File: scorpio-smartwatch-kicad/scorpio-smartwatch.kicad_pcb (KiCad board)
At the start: 2 copper layers, 5 parts, among them IC1 LSM6DSV80XTR, U1 nRF52840, U2 MIA-M10Q, U3 LIS2MDL

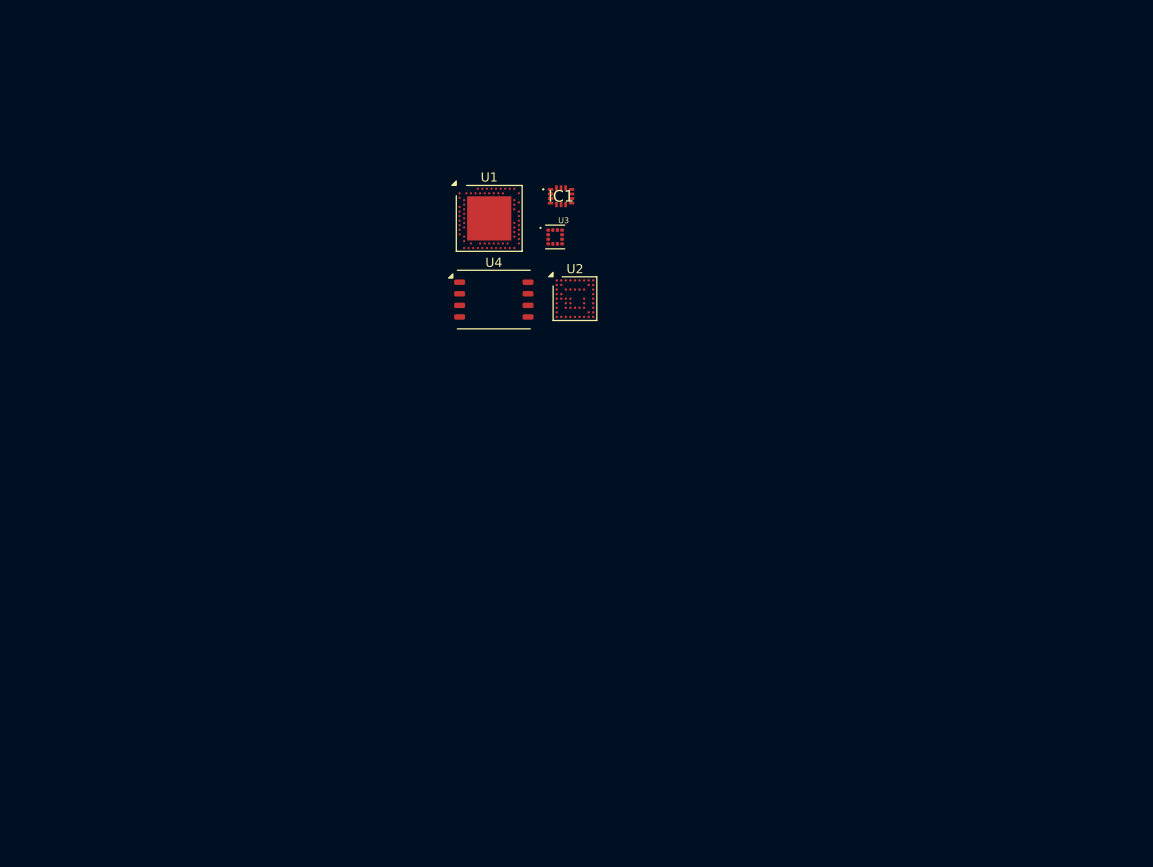
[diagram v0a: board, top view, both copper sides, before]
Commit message: Adding dimensions on the pcb and adding tables for current and battery sizes. need to change NRF footprint still. Need to add: Buttons, Screen Connector / Driver, HR connector (I2C), Power Management, Battery Connector, Mounting Holes, Passives.
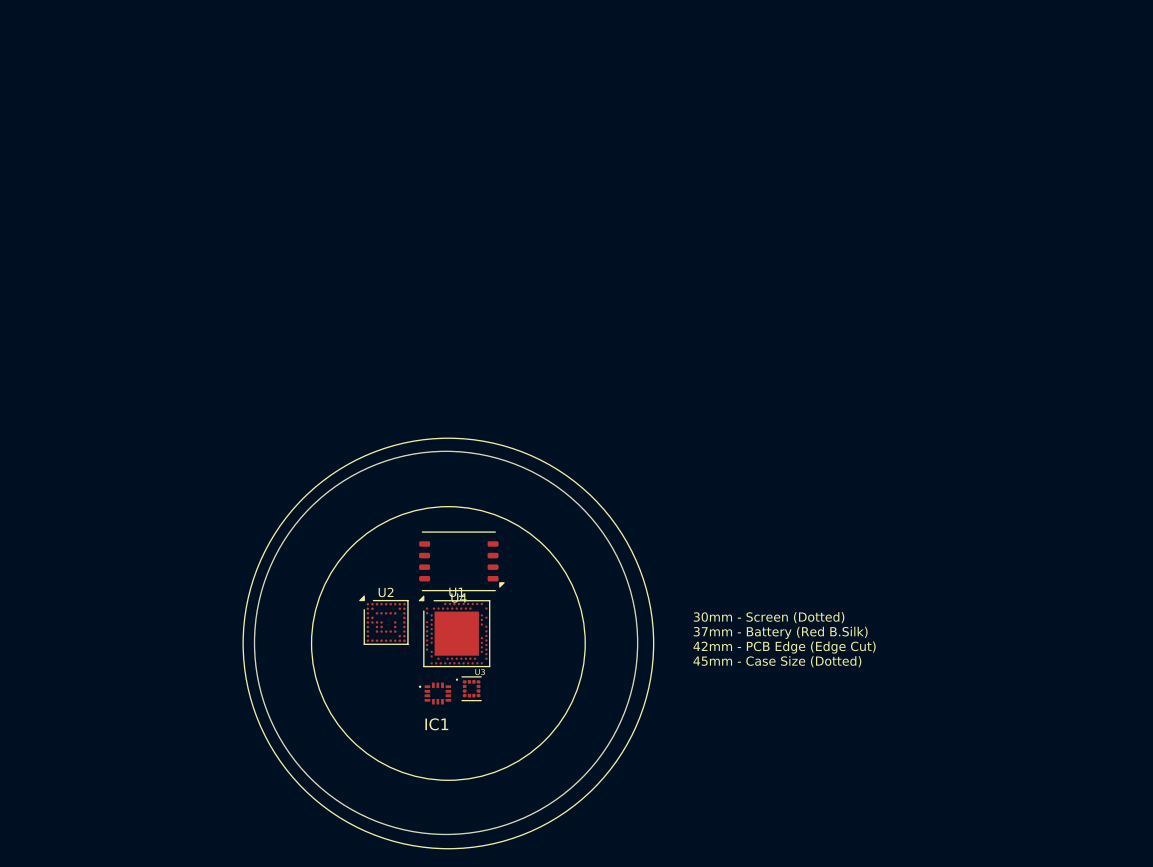
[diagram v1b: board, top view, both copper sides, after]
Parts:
- moved IC1 56.2 mm to (126.1, 132.7)
- moved U3 50.4 mm to (129.8, 132.2)
- moved U1 45.7 mm to (128.2, 126.2)
- moved U2 41.1 mm to (120.4, 124.9)
- moved U4 29.0 mm to (128.4, 118.2), turned to 180 degrees
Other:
- board outline added: 42 x 42 mm
- board text added: "30mm - Screen (Dotted) 37mm - Battery (Red B.Silk) 42mm - PCB Edge (Edge Cut) 45mm - Case Size (Dotted)"
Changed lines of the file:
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@@
 	(footprint "Package_LGA:ublox_LGA-53_4.5x4.5mm_Layout9x9_P0.5mm"
 		(layer "F.Cu")
-		(at 141.129 89.44)
+		(at 120.428 124.936)
 		(descr "ublox MIA SoC Module, 4.5x4.5mm, 53 Ball, 9x9 Layout, 0.5mm Pitch, generated with kicad-footprint-generator ipc_bga_generator.py, https://content.u-blox.com/sites/default/files/documents/MIA-M10Q_IntegrationManual_UBX-21028173.pdf#page=82")
 		(tags "LGA 53 0.5 ublox_MIA-M-LGA53")
@@
 	(footprint "Package_DFN_QFN:Nordic_AQFN-73-1EP_7x7mm_P0.5mm"
 		(layer "F.Cu")
-		(at 131.729 80.64)
+		(at 128.171 126.163)
 		(descr "http://infocenter.nordicsemi.com/index.jsp?topic=%2Fcom.nordic.infocenter.nrf52%2Fdita%2Fnrf52%2Fchips%2Fnrf52840.html")
 		(tags "AQFN 7mm ")
@@
 	(footprint "ZDSD16GLGIAG:LGA-8_8x6.2mm_P1.27mm"
 		(layer "F.Cu")
-		(at 132.234 89.54)
+		(at 128.397 118.237 180)
 		(descr "LGA, 8 Pin (https://datasheet.lcsc.com/lcsc/2303241700_Zetta-ZDSD64GLGEAG-R_C5277948.pdf#page=17), generated with kicad-footprint-generator ipc_noLead_generator.py")
 		(tags "LGA NoLead")
@@
 		(attr smd)
 		(fp_line
+			(start -4 3.21)
+			(end 4 3.21)
+			(stroke
+				(width 0.12)
+				(type solid)
+			)
+			(layer "F.SilkS")
+		)
+		(fp_line
 			(start -4 -3.21)
 			(end 4 -3.21)
-			(stroke
-				(width 0.12)
-				(type solid)
-			)
-			(layer "F.SilkS")
-		)
-		(fp_line
-			(start -4 3.21)
-			(end 4 3.21)
 			(stroke
 				(width 0.12)
@@
 		)
 		(fp_line
+			(start 4.6 2.46)
+			(end 4.25 2.46)
+			(stroke
+				(width 0.05)
+				(type solid)
+			)
+			(layer "F.CrtYd")
+		)
+		(fp_line
+			(start 4.6 -2.46)
+			(end 4.6 2.46)
+			(stroke
+				(width 0.05)
+				(type solid)
+			)
+			(layer "F.CrtYd")
+		)
+		(fp_line
+			(start 4.25 3.35)
+			(end -4.25 3.35)
+			(stroke
+				(width 0.05)
+				(type solid)
+			)
+			(layer "F.CrtYd")
+		)
+		(fp_line
+			(start 4.25 2.46)
+			(end 4.25 3.35)
+			(stroke
+				(width 0.05)
+				(type solid)
+			)
+			(layer "F.CrtYd")
+		)
+		(fp_line
+			(start 4.25 -2.46)
+			(end 4.6 -2.46)
+			(stroke
+				(width 0.05)
+				(type solid)
+			)
+			(layer "F.CrtYd")
+		)
+		(fp_line
+			(start 4.25 -3.35)
+			(end 4.25 -2.46)
+			(stroke
+				(width 0.05)
+				(type solid)
+			)
+			(layer "F.CrtYd")
+		)
+		(fp_line
+			(start -4.25 3.35)
+			(end -4.25 2.46)
+			(stroke
+				(width 0.05)
+				(type solid)
+			)
+			(layer "F.CrtYd")
+		)
+		(fp_line
+			(start -4.25 2.46)
+			(end -4.6 2.46)
+			(stroke
+				(width 0.05)
+				(type solid)
+			)
+			(layer "F.CrtYd")
+		)
+		(fp_line
+			(start -4.25 -2.46)
+			(end -4.25 -3.35)
+			(stroke
+				(width 0.05)
+				(type solid)
+			)
+			(layer "F.CrtYd")
+		)
+		(fp_line
+			(start -4.25 -3.35)
+			(end 4.25 -3.35)
+			(stroke
+				(width 0.05)
+				(type solid)
+			)
+			(layer "F.CrtYd")
+		)
+		(fp_line
+			(start -4.6 2.46)
+			(end -4.6 -2.46)
+			(stroke
+				(width 0.05)
+				(type solid)
+			)
+			(layer "F.CrtYd")
+		)
+		(fp_line
 			(start -4.6 -2.46)
 			(end -4.25 -2.46)
-			(stroke
-				(width 0.05)
-				(type solid)
-			)
-			(layer "F.CrtYd")
-		)
-		(fp_line
-			(start -4.6 2.46)
-			(end -4.6 -2.46)
-			(stroke
-				(width 0.05)
-				(type solid)
-			)
-			(layer "F.CrtYd")
-		)
-		(fp_line
-			(start -4.25 -3.35)
-			(end 4.25 -3.35)
-			(stroke
-				(width 0.05)
-				(type solid)
-			)
-			(layer "F.CrtYd")
-		)
-		(fp_line
-			(start -4.25 -2.46)
-			(end -4.25 -3.35)
-			(stroke
-				(width 0.05)
-				(type solid)
-			)
-			(layer "F.CrtYd")
-		)
-		(fp_line
-			(start -4.25 2.46)
-			(end -4.6 2.46)
-			(stroke
-				(width 0.05)
-				(type solid)
-			)
-			(layer "F.CrtYd")
-		)
-		(fp_line
-			(start -4.25 3.35)
-			(end -4.25 2.46)
-			(stroke
-				(width 0.05)
-				(type solid)
-			)
-			(layer "F.CrtYd")
-		)
-		(fp_line
-			(start 4.25 -3.35)
-			(end 4.25 -2.46)
-			(stroke
-				(width 0.05)
-				(type solid)
-			)
-			(layer "F.CrtYd")
-		)
-		(fp_line
-			(start 4.25 -2.46)
-			(end 4.6 -2.46)
-			(stroke
-				(width 0.05)
-				(type solid)
-			)
-			(layer "F.CrtYd")
-		)
-		(fp_line
-			(start 4.25 2.46)
-			(end 4.25 3.35)
-			(stroke
-				(width 0.05)
-				(type solid)
-			)
-			(layer "F.CrtYd")
-		)
-		(fp_line
-			(start 4.25 3.35)
-			(end -4.25 3.35)
-			(stroke
-				(width 0.05)
-				(type solid)
-			)
-			(layer "F.CrtYd")
-		)
-		(fp_line
-			(start 4.6 -2.46)
-			(end 4.6 2.46)
-			(stroke
-				(width 0.05)
-				(type solid)
-			)
-			(layer "F.CrtYd")
-		)
-		(fp_line
-			(start 4.6 2.46)
-			(end 4.25 2.46)
 			(stroke
 				(width 0.05)
@@
 		)
 		(pad "1" smd roundrect
-			(at -3.75 -1.905)
+			(at -3.75 -1.905 180)
 			(size 1.2 0.6)
 			(layers "F.Cu" "F.Mask" "F.Paste")
@@
 		)
 		(pad "2" smd roundrect
-			(at -3.75 -0.635)
+			(at -3.75 -0.635 180)
 			(size 1.2 0.6)
 			(layers "F.Cu" "F.Mask" "F.Paste")
@@
 		)
 		(pad "3" smd roundrect
-			(at -3.75 0.635)
+			(at -3.75 0.635 180)
 			(size 1.2 0.6)
 			(layers "F.Cu" "F.Mask" "F.Paste")
@@
 		)
 		(pad "4" smd roundrect
-			(at -3.75 1.905)
+			(at -3.75 1.905 180)
 			(size 1.2 0.6)
 			(layers "F.Cu" "F.Mask" "F.Paste")
@@
 		)
 		(pad "5" smd roundrect
-			(at 3.75 1.905)
+			(at 3.75 1.905 180)
 			(size 1.2 0.6)
 			(layers "F.Cu" "F.Mask" "F.Paste")
@@
 		)
 		(pad "6" smd roundrect
-			(at 3.75 0.635)
+			(at 3.75 0.635 180)
 			(size 1.2 0.6)
 			(layers "F.Cu" "F.Mask" "F.Paste")
@@
 		)
 		(pad "7" smd roundrect
-			(at 3.75 -0.635)
+			(at 3.75 -0.635 180)
 			(size 1.2 0.6)
 			(layers "F.Cu" "F.Mask" "F.Paste")
@@
 		)
 		(pad "8" smd roundrect
-			(at 3.75 -1.905)
+			(at 3.75 -1.905 180)
 			(size 1.2 0.6)
 			(layers "F.Cu" "F.Mask" "F.Paste")
@@
 	(footprint "LIS2MDL:PQFN50P200X200X70-12N"
 		(layer "F.Cu")
-		(at 138.954 82.6785)
+		(at 129.798 132.205)
 		(property "Reference" "U3"
 			(at 0.932 -1.8064 0)
@@
 		)
 		(property "Value" "LIS2MDL"
-			(at 7.2344 1.7936 0)
+			(at 0.885 2.034 0)
 			(layer "F.Fab")
 			(effects
@@
 	(footprint "LSM6DSV80X:LSM6DSV16BXTR"
 		(layer "F.Cu")
-		(at 139.604 78.215)
+		(at 126.103 132.726)
 		(descr "LGA-14L 2.5 x 3.0 x 0.74 mm XDM)")
 		(tags "Integrated Circuit")
 		(property "Reference" "IC1"
-			(at 0 0 0)
+			(at -0.12 3.425 0)
 			(layer "F.SilkS")
 			(effects
@@
 		)
 		(fp_text user "${REFERENCE}"
-			(at 0 0 0)
+			(at 0.007 3.552 0)
 			(layer "F.Fab")
 			(effects
@@
 		)
 	)
+	(gr_circle
+		(center 127.254 127.24)
+		(end 142.254 127.24)
+		(stroke
+			(width 0.1)
+			(type dot)
+		)
+		(fill no)
+		(layer "F.SilkS")
+	)
+	(gr_circle
+		(center 127.254 127.24)
+		(end 149.754 127.24)
+		(stroke
+			(width 0.1)
+			(type dot)
+		)
+		(fill no)
+		(layer "F.SilkS")
+	)
+	(gr_circle
+		(center 127.254 127.24)
+		(end 144.754 127.24)
+		(stroke
+			(width 0.1)
+			(type solid)
+		)
+		(fill no)
+		(layer "B.SilkS")
+	)
+	(gr_circle
+		(center 127.254 127.24)
+		(end 145.754 127.24)
+		(stroke
+			(width 0.1)
+			(type solid)
+		)
+		(fill no)
+		(layer "B.SilkS")
+	)
+	(gr_circle
+		(center 127 127.1765)
+		(end 148 127.1765)
+		(stroke
+			(width 0.05)
+			(type solid)
+		)
+		(fill no)
+		(layer "Edge.Cuts")
+	)
+	(gr_text "30mm - Screen (Dotted)\n37mm - Battery (Red B.Silk)\n42mm - PCB Edge (Edge Cut)\n45mm - Case Size (Dotted)"
+		(at 154.051 129.794 0)
+		(layer "F.SilkS")
+		(effects
+			(font
+				(size 1 1)
+				(thickness 0.1)
+			)
+			(justify left bottom)
+		)
+	)

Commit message: minor changes
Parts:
- removed U1: nRF52840, Package_DFN_QFN:Nordic_AQFN-73-1EP_7x7mm_P0.5mm
- added IC2: NRF52840-QFAA-F-R, RF_Module:QFN40P600X600X95-49N-D, F.Cu at (128.5, 126.0)

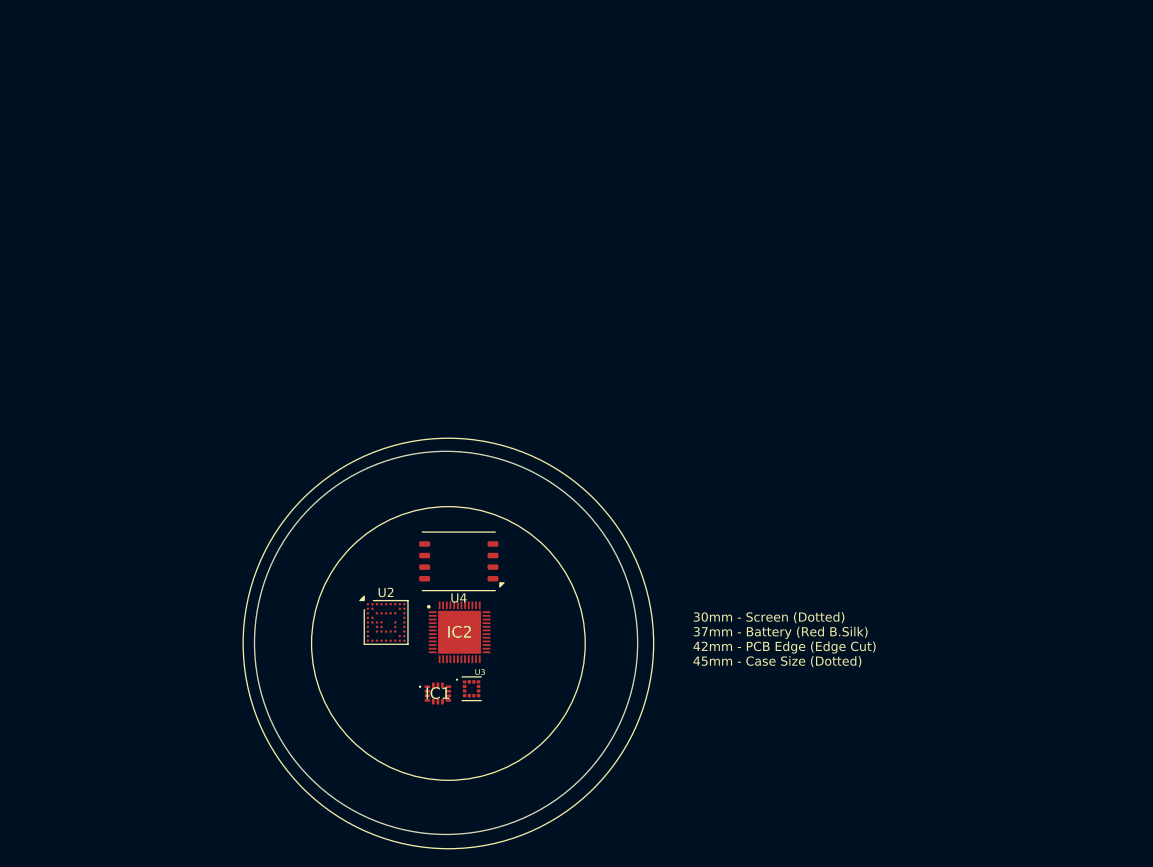
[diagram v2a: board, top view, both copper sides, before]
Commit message: wip commit, added chip antenna, trying out different pcb sizes. not routing until we can figure out the rf nightmare with ground plane sizes.
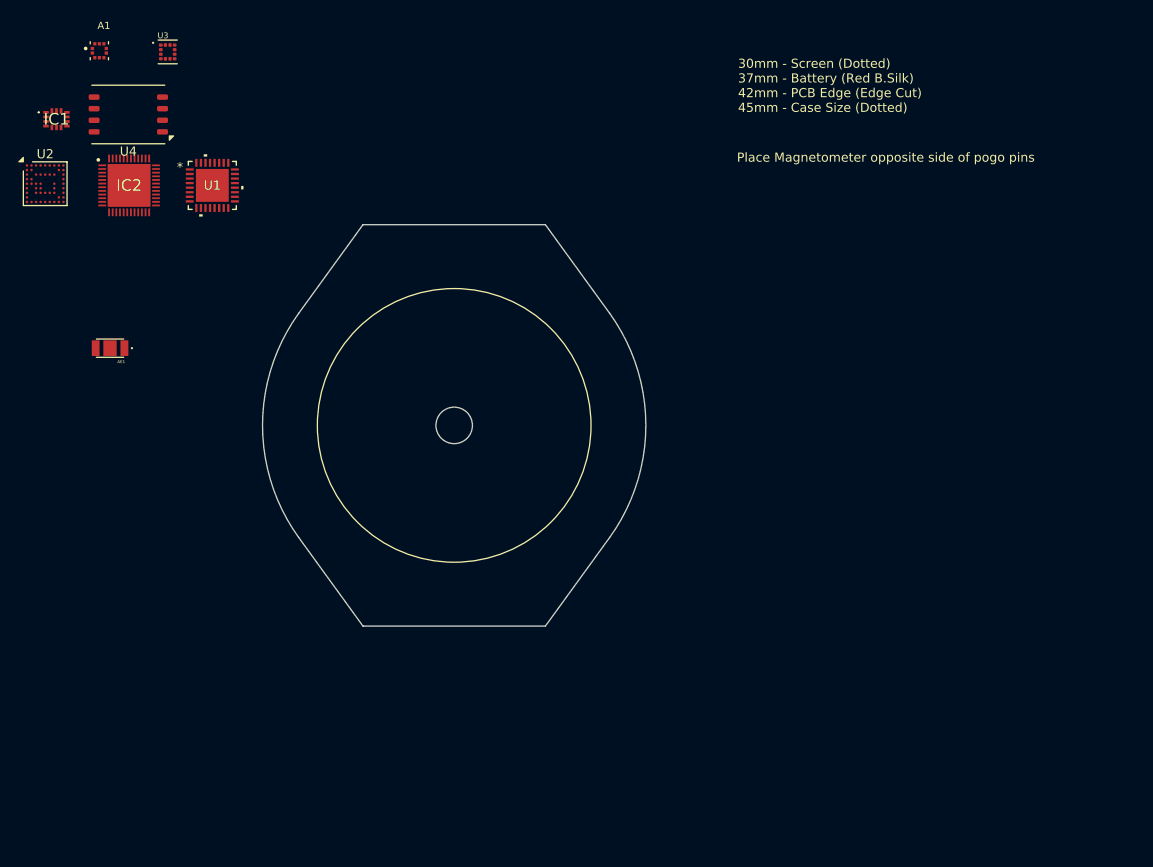
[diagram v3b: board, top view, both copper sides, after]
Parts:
- added A1: LPS22DFTR, LPS22DF:XDCR_LPS22DFTR, F.Cu at (89.0, 62.3)
- added AE1: GWLA.01, GWLA01:TOAGLAS_GWLA.01, F.Cu at (90.2, 94.9)
- added U1: NPM1300-QEAA-R7, NPM1300:QFN32_5X5_NOR-M, F.Cu at (101.4, 77.0)
- moved U3 77.4 mm to (96.5, 62.4)
- moved IC1 75.6 mm to (84.3, 69.8)
- moved IC2 60.9 mm to (92.3, 77.0)
- moved U4 60.9 mm to (92.2, 69.3)
- moved U2 60.9 mm to (83.1, 76.8)
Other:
- board size 42 x 42 mm -> 42 x 44 mm
- board text added: "3 SPI - SD SPI - MEMS SPI - Display QSPI 1 UART - GPS 1 I2C - HR Sensor - PMIC 1 SWD/JTAG - Programming 2 RFE - BLE - GPS"
- board text added: "KOZ ANT"
- board text added: "Place Magnetometer opposite side of pogo pins"
